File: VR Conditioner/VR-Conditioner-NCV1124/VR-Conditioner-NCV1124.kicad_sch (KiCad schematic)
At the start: 9 parts, among them J1 NCV1124DR2G, J2 Board Conn

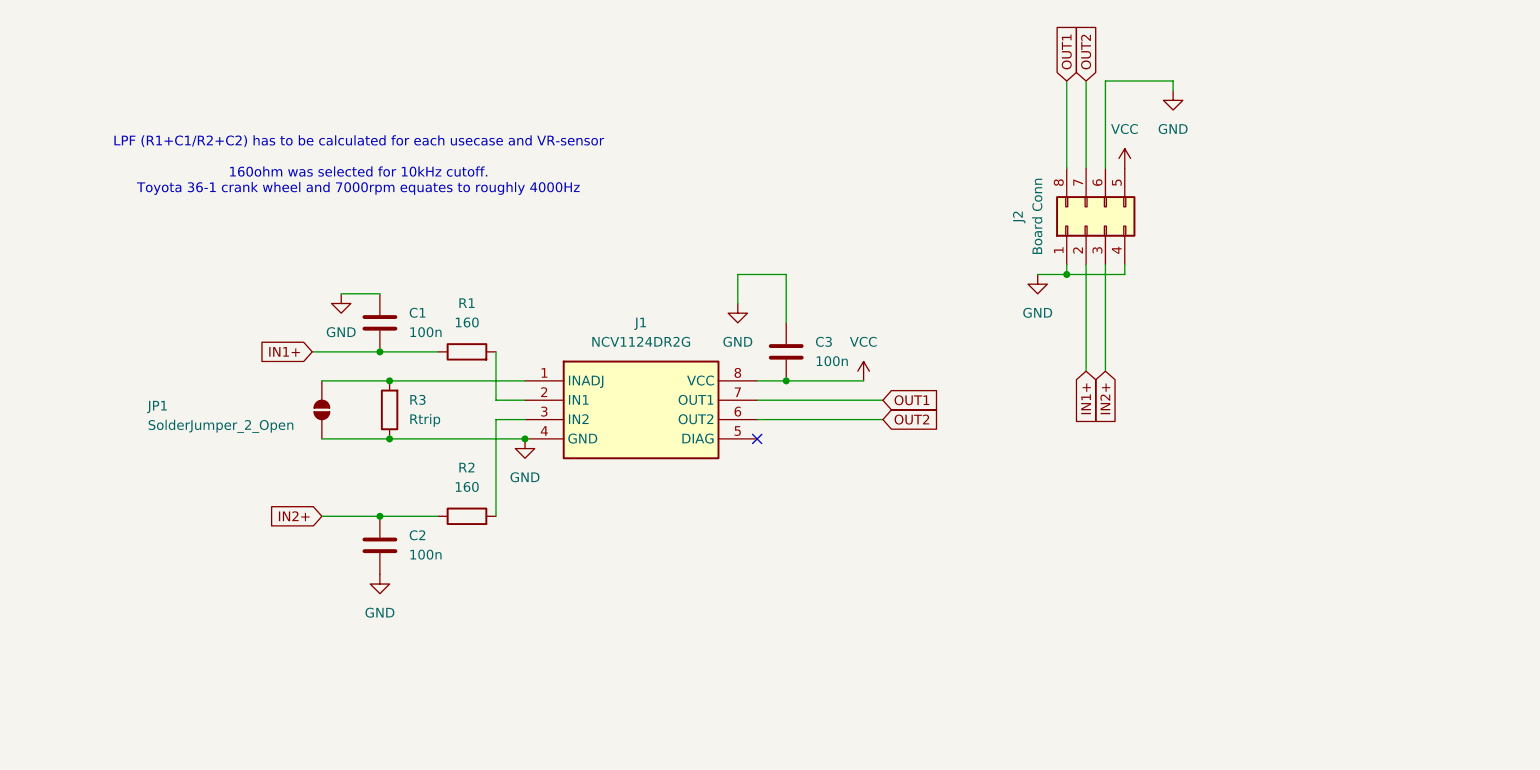
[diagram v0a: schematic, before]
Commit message: Changed to THT resistors due to wattage requirements as per ncv1124 datasheet. Added prod files
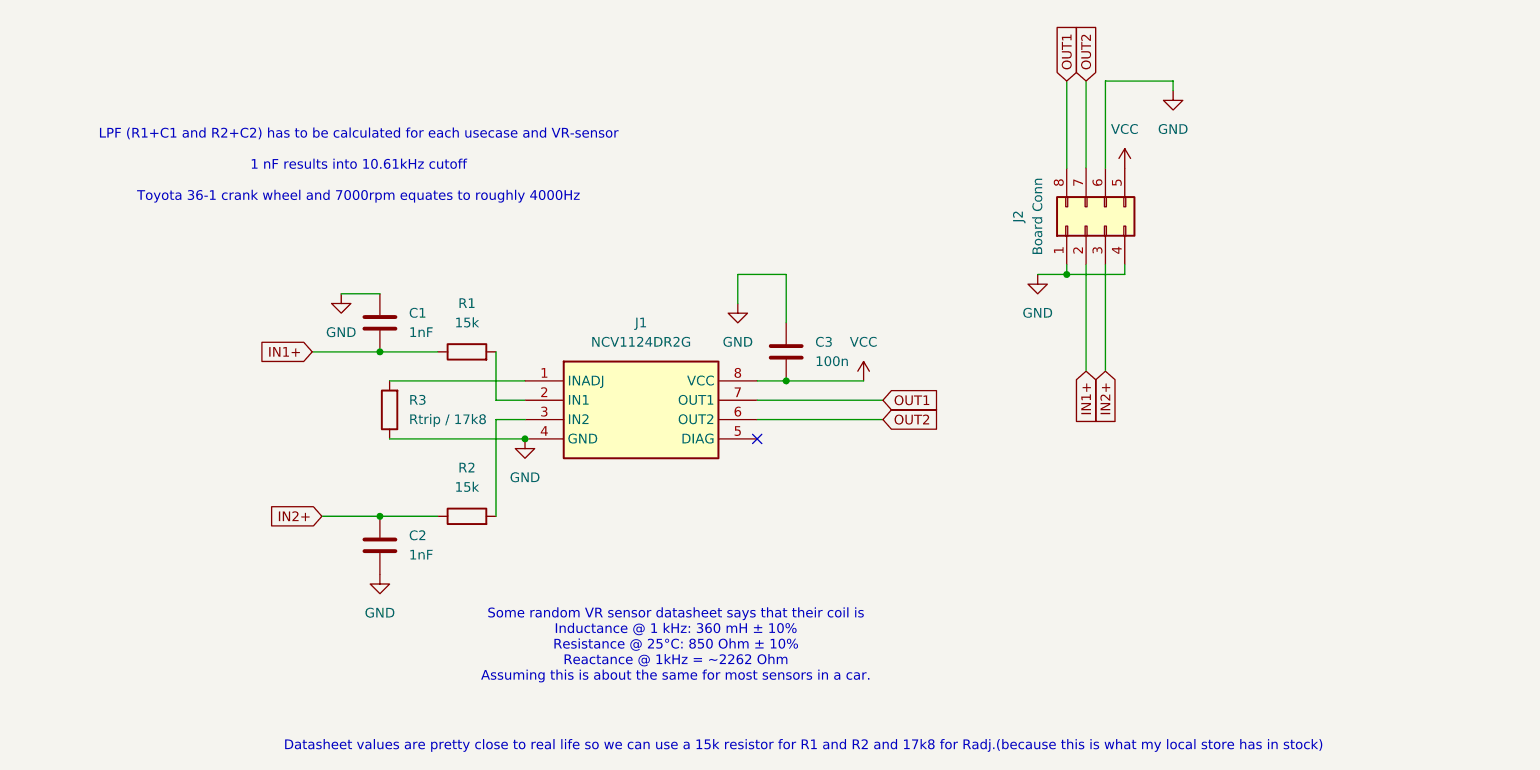
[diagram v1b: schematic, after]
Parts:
- removed JP1: SolderJumper_2_Open, Jumper:SolderJumper-2_P1.3mm_Open_RoundedPad1.0x1.5mm, symbol Jumper:SolderJumper_2_Open
- C1, C2: value 100n -> 1nF; footprint Capacitor_SMD:C_0805_2012Metric_Pad1.18x1.45mm_HandSolder -> Capacitor_SMD:C_1206_3216Metric_Pad1.33x1.80mm_HandSolder
- C3: footprint Capacitor_SMD:C_0805_2012Metric_Pad1.18x1.45mm_HandSolder -> Capacitor_SMD:C_1206_3216Metric_Pad1.33x1.80mm_HandSolder
- R1, R2: value 160 -> 15k; footprint Capacitor_SMD:C_0805_2012Metric_Pad1.18x1.45mm_HandSolder -> Resistor_THT:R_Axial_DIN0207_L6.3mm_D2.5mm_P10.16mm_Horizontal
- R3: value Rtrip -> Rtrip / 17k8; footprint Capacitor_SMD:C_0805_2012Metric_Pad1.18x1.45mm_HandSolder -> Resistor_THT:R_Axial_DIN0207_L6.3mm_D2.5mm_P10.16mm_Horizontal
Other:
- note added: "Datasheet values are pretty close to real life so we can use a 15k resistor for R1 and R2 and 17k8 for Radj.(because this is what my local store has in stock)"
- note added: "LPF (R1+C1 and R2+C2) has to be calculated for each usecase and VR-sensor 1 nF results into 10.61kHz cutoff Toyota 36-1 crank wheel and 7000rpm equates to roughly 4000Hz"
- note added: "Some random VR sensor datasheet says that their coil is Inductance @ 1 kHz: 360 mH ± 10% Resistance @ 25°C: 850 Ohm ± 10% Reactance @ 1kHz = ~2262 Ohm Assuming this is about the same for most sensors in a car."
- note removed: "LPF (R1+C1/R2+C2) has to be calculated for each usecase and VR-sensor 160ohm was selected for 10kHz cutoff. Toyota 36-1 crank wheel and 7000rpm equates to roughly 4000Hz"
